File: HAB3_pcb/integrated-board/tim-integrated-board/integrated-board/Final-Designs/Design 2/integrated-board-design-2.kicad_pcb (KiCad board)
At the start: 2 copper layers, 145 x 125.7 mm, 122 parts, among them IC1 RTC_PCF8523T, J1 Conn_01x02_Male, J1 Conn_01x03_Male, J1 Conn_01x09_Female, J1 Conn_ARM_JTAG_SWD_20, J10 Conn_01x02_Male, J12 Conn_01x03_Male, J13 Conn_01x04_Male, J14 Conn_01x05_Male, J15 Conn_01x08_Male, J2 Conn_01x02_Female, J2 Conn_01x05_Female, J2 Conn_01x06_Male, J2 Micro_SD_Card_Det, J3 Conn_01x16_Male, J4 Conn_01x16_Male, J5 Conn_01x16_Male, J6 Conn_01x02_Male, J7 Conn_01x02_Male, J8 Conn_01x02_Male, J9 Conn_01x11_Male, Q1 32.768KHz, SW1 SW_DPST_x2, U1 FGPMMOPA6H, U1 ICM-20689, U1 LSM9DS0, U1 MAX31855, U1 MS560702BA03-00, U1 STM32F401RET6, U2 TPS564208, U3 TPS564208, Y1 32.768MHz

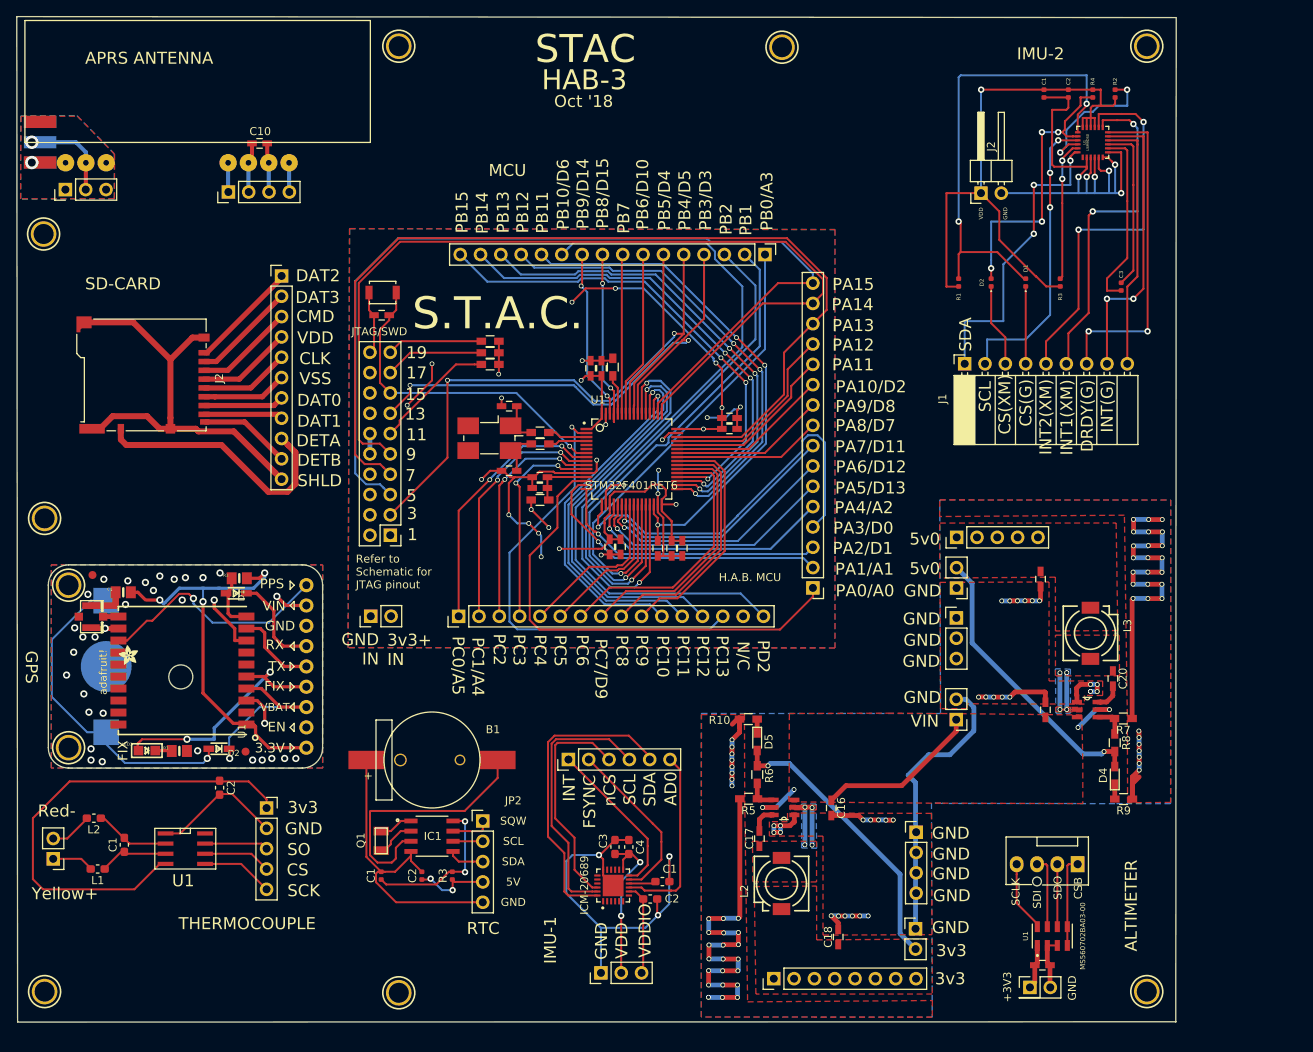
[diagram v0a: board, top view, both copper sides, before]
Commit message: final pcb design complete with InstantDFM
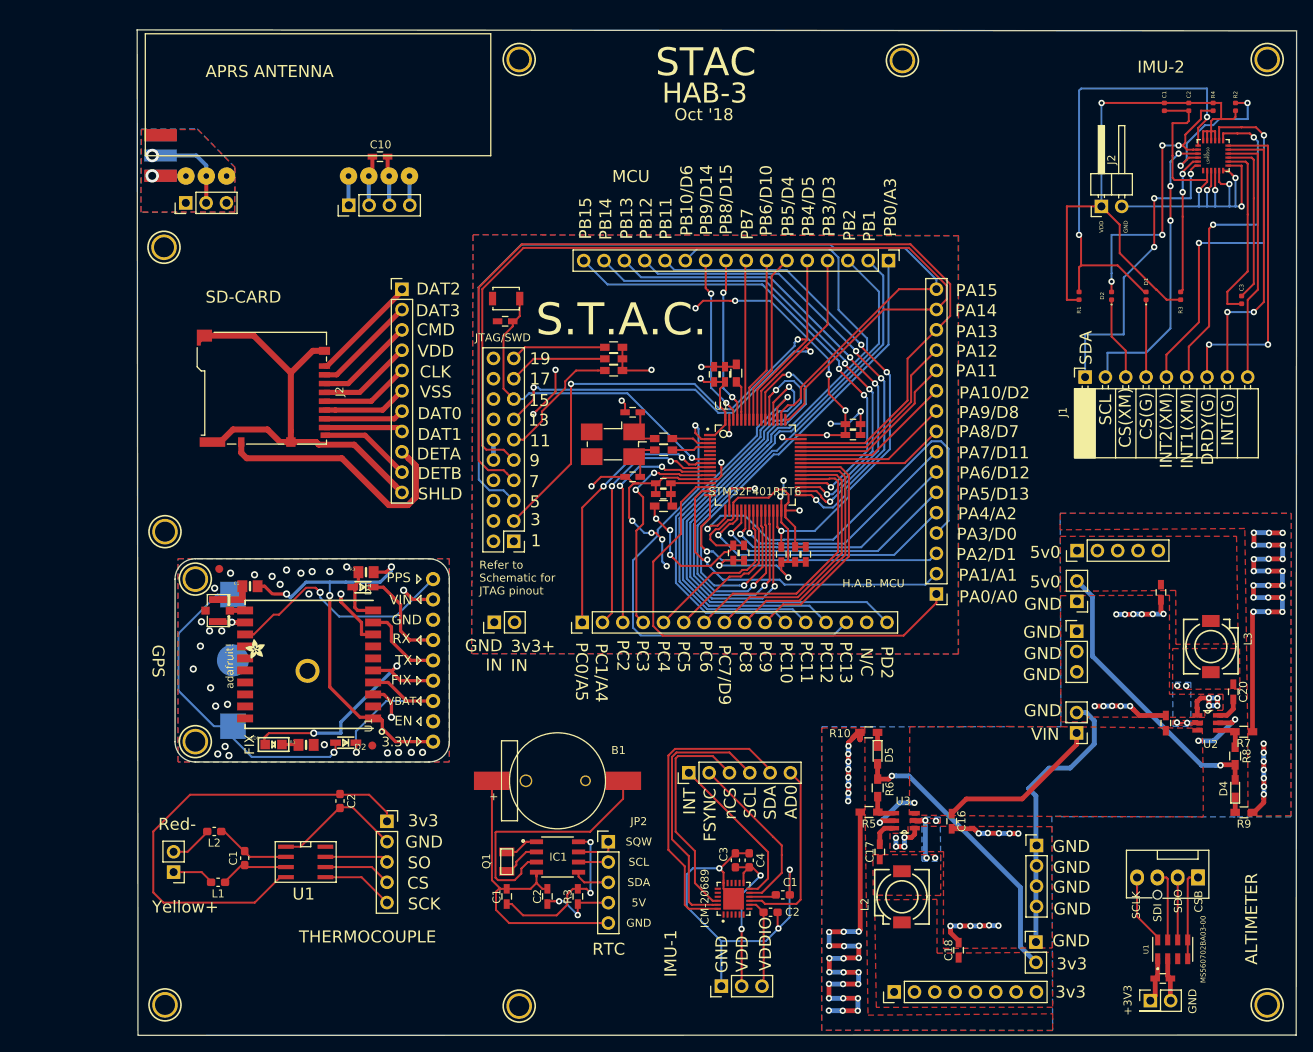
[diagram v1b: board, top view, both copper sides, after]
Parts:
- C1, C2: footprint Capacitor_SMD:C_0402_1005Metric -> Capacitors_SMD:C_0603_HandSoldering
- R3: footprint Resistor_SMD:R_0402_1005Metric -> Capacitors_SMD:C_0603_HandSoldering
- moved JP2 15.9 mm to (132.0, 130.6)
- moved B1 15.9 mm to (125.6, 122.9)
- moved C1 15.9 mm to (119.3, 137.4)
- moved C2 15.9 mm to (124.4, 137.4)
- moved IC1 15.9 mm to (125.6, 132.5)
- moved Q1 15.9 mm to (119.3, 133.1)
- moved R3 15.9 mm to (128.2, 137.4)
- moved C1 15.9 mm to (87.2, 98.6)
- moved D2 15.9 mm to (99.2, 118.2)
- moved FID1 15.9 mm to (83.4, 96.5)
- moved FID2 15.9 mm to (102.5, 118.5)
- moved JP1 15.9 mm to (110.1, 107.9)
- moved LED1 15.9 mm to (90.1, 118.4)
- moved R1 15.9 mm to (94.2, 118.5)
- moved U$15 15.9 mm to (89.1, 107.7)
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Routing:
- net GND: track 207.1 -> 220.8 mm, vias 53 -> 52
- net +3V3: track 149.6 -> 158.8 mm
- net Net-(C20-Pad1): track 11.3 -> 2.13 mm
- net PD2: track 60.2 -> 68.1 mm
- net PC12: track 51.2 -> 58.7 mm
- net PC11: track 47.5 -> 53.9 mm
- net PB10: track 87.6 -> 93.5 mm
- net PB2: track 65.7 -> 71.4 mm
- net Net-(C17-Pad1): track 11.7 -> 6.06 mm
- net PC10: track 43.1 -> 48.1 mm
- net PB0: track 60.7 -> 65.5 mm
- net PB1: track 63.9 -> 68.2 mm
- net PA1: track 38.0 -> 41.7 mm
- net PA4: track 31.9 -> 34.8 mm
- net PA2: track 34.6 -> 37.3 mm
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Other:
- outline, holes or cut-outs redrawn
- copper layers 2 -> 4
- net class Default: via_dia 0.6 -> 0.8
- board text added: "U2"
- board text added: "U3"

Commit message: final final pcb design complete with InstantDFM
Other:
- copper layers 4 -> 2
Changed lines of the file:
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@@
   (layers
     (0 F.Cu signal)
-    (1 In1.Cu power)
-    (2 In2.Cu power)
     (31 B.Cu signal)
     (32 B.Adhes user)
